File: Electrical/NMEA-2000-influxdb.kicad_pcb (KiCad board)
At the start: 4 copper layers, 9 parts, among them J1 Conn_01x02, J2 Conn_01x02, U1 LM7805_TO220, U2 SN65HVD230-Module, U3 RTC-Module, U4 ESP32-DevKitC, U5 SD-Card-Module

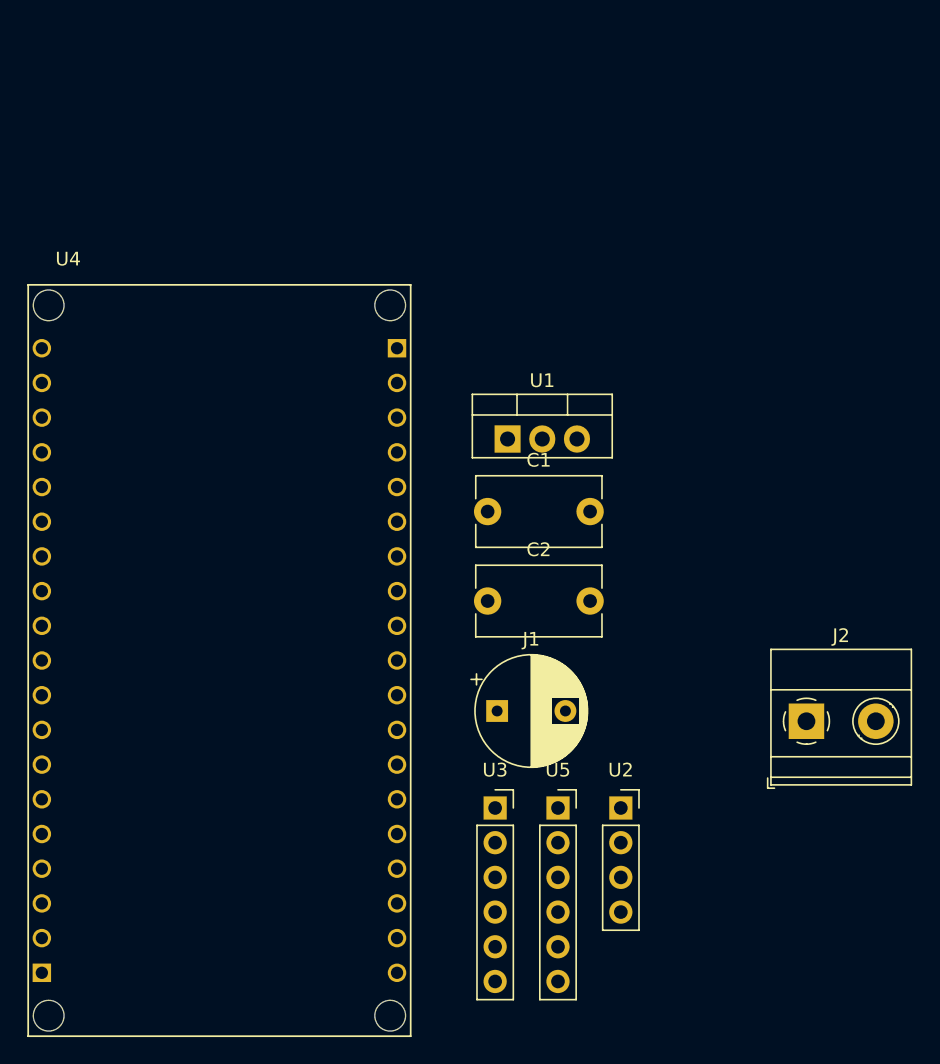
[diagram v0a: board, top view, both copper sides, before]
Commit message: Replaced SN65HVD230-Module with SN65HVD230
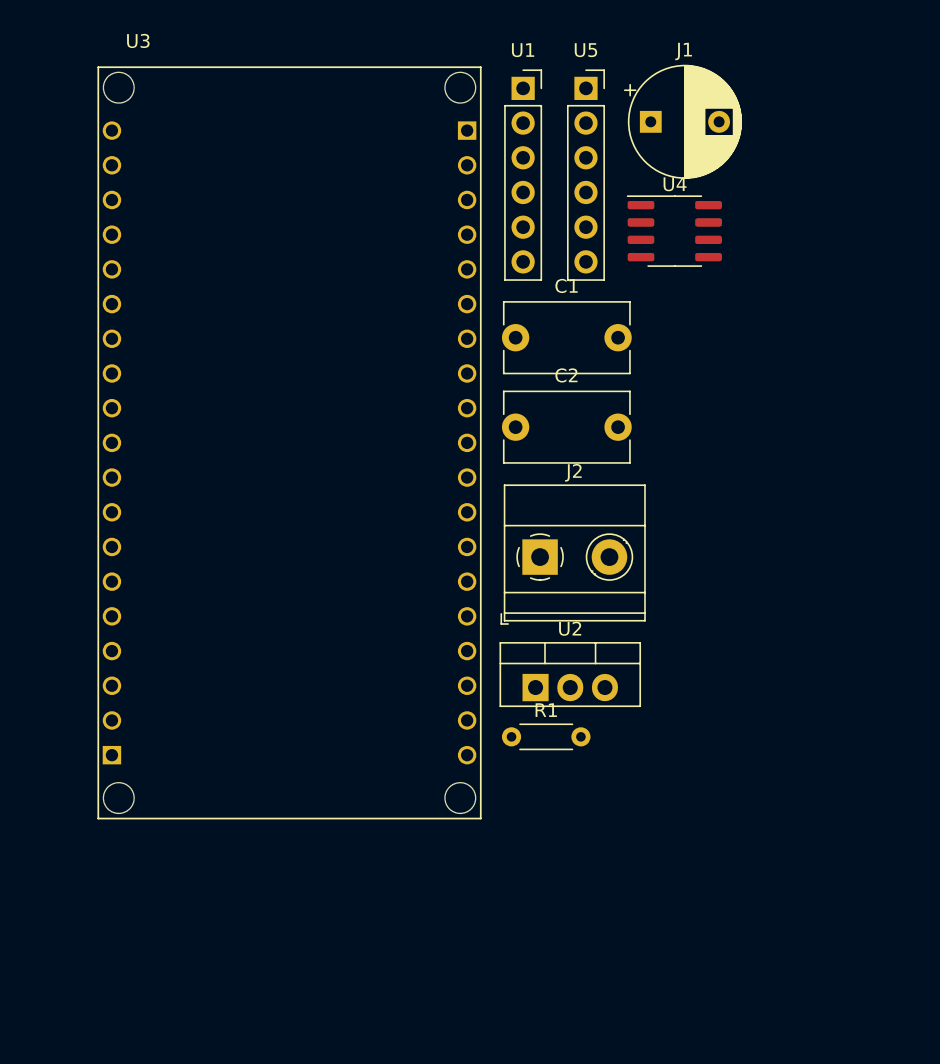
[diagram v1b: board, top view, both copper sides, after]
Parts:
- added R1: R, Resistor_THT:R_Axial_DIN0204_L3.6mm_D1.6mm_P5.08mm_Horizontal, F.Cu at (123.8, 102.9)
- U1: value LM7805_TO220 -> SD-Card-Module; footprint Package_TO_SOT_THT:TO-220-3_Vertical -> Connector_PinSocket_2.54mm:PinSocket_1x06_P2.54mm_Vertical
- U2: value SN65HVD230-Module -> LM7805_TO220; footprint Connector_PinSocket_2.54mm:PinSocket_1x04_P2.54mm_Vertical -> Package_TO_SOT_THT:TO-220-3_Vertical
- U3: value RTC-Module -> ESP32-DevKitC; footprint Connector_PinSocket_2.54mm:PinSocket_1x06_P2.54mm_Vertical -> Espressif:MODULE_ESP32_NODEMCU
- U4: value ESP32-DevKitC -> SN65HVD230; footprint Espressif:MODULE_ESP32_NODEMCU -> Package_SO:SOIC-8_3.9x4.9mm_P1.27mm
- U5: value SD-Card-Module -> RTC-Module
- moved U5 52.7 mm to (129.3, 55.4)
- moved U4 45.8 mm to (135.8, 65.8)
- moved J1 44.6 mm to (134.0, 57.9)
- moved U3 30.7 mm to (107.6, 81.3)
- moved U1 25.7 mm to (124.7, 55.4)
- moved J2 22.9 mm to (125.9, 89.7)
- moved C2 12.9 mm to (124.1, 80.2)
- moved C1 12.9 mm to (124.1, 73.7)
- moved U2 10.8 mm to (125.6, 99.3)
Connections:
- U1 pad 1: +12V -> GND
- U1 pad 2: GND -> +5V
- U1 pad 3: +5V -> /MISO
- U2 pad 1: +3V3 -> +12V
- U2 pad 3: /CAN_RX -> +5V
- U5 pad 1: GND -> +5V
- U5 pad 2: +5V -> GND
- U5 pad 3: /MISO -> (no net)
- U5 pad 4: /MOSI -> /SCL
- U5 pad 5: /SCK -> unconnected-(U5-SQW-Pad5)
- U5 pad 6: /CS -> unconnected-(U5-32K-Pad6)

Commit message: Added board
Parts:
- J1: value Conn_01x02 -> Conn_01x04; footprint Capacitor_THT:CP_Radial_D8.0mm_P5.00mm -> TerminalBlock_Phoenix:TerminalBlock_Phoenix_MKDS-1,5-4-5.08_1x04_P5.08mm_Horizontal
- J2: value Conn_01x02 -> Conn_01x04; footprint TerminalBlock_Phoenix:TerminalBlock_Phoenix_MKDS-1,5-2-5.08_1x02_P5.08mm_Horizontal -> Connector_PinSocket_2.54mm:PinSocket_1x04_P2.54mm_Horizontal
- U1, U5: footprint Connector_PinSocket_2.54mm:PinSocket_1x06_P2.54mm_Vertical -> Connector_PinSocket_2.54mm:PinSocket_1x06_P2.54mm_Horizontal
- U3: value ESP32-DevKitC -> ESP32_NODEMCU; footprint Espressif:MODULE_ESP32_NODEMCU -> esp32:esp32
- moved U2 59.6 mm to (109.2, 41.9), turned to -90 degrees
- moved U1 46.9 mm to (153.1, 92.7), turned to 180 degrees
- moved U4 45.3 mm to (100.3, 94.0)
- moved J1 39.6 mm to (97.8, 41.9), turned to -90 degrees
- moved J2 31.8 mm to (102.2, 68.5)
- moved R1 26.1 mm to (97.8, 104.1)
- moved U3 26.1 mm to (132.1, 72.4), turned to 90 degrees
- moved U5 24.8 mm to (153.1, 62.2), turned to 180 degrees
- moved C1 21.5 mm to (114.2, 54.6), turned to 180 degrees
- moved C2 19.4 mm to (114.2, 63.5), turned to 180 degrees
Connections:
- J1 pad 2: GND -> CAN_L
- J2 pad 1: Net-(J2-Pin_1) -> +5V
- J2 pad 2: Net-(J2-Pin_2) -> /RX
- U4 pad 6: Net-(J2-Pin_2) -> CAN_L
- U4 pad 7: Net-(J2-Pin_1) -> CAN_H
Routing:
- net /CAN_RX: track 0.00 -> 59.8 mm, vias 0 -> 1
- net CAN_L: track 0.00 -> 57.7 mm
- net /CAN_TX: track 0.00 -> 56.5 mm, vias 0 -> 1
- net CAN_H: track 0.00 -> 47.4 mm
- net /SCL: track 0.00 -> 46.0 mm
- net /MISO: track 0.00 -> 34.4 mm
- net /MOSI: track 0.00 -> 34.4 mm
- net /CS: track 0.00 -> 34.3 mm
- net +12V: track 0.00 -> 27.0 mm
- net /SCK: track 0.00 -> 13.6 mm
- net Net-(U4-Rs): track 0.00 -> 12.1 mm, vias 0 -> 1
- net +3.3V: track 0.00 -> 11.1 mm
- added copper zone on B.Cu, net +5V
- added copper zone on F.Cu, net GND
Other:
- board outline added: 114.3 x 71.1 mm

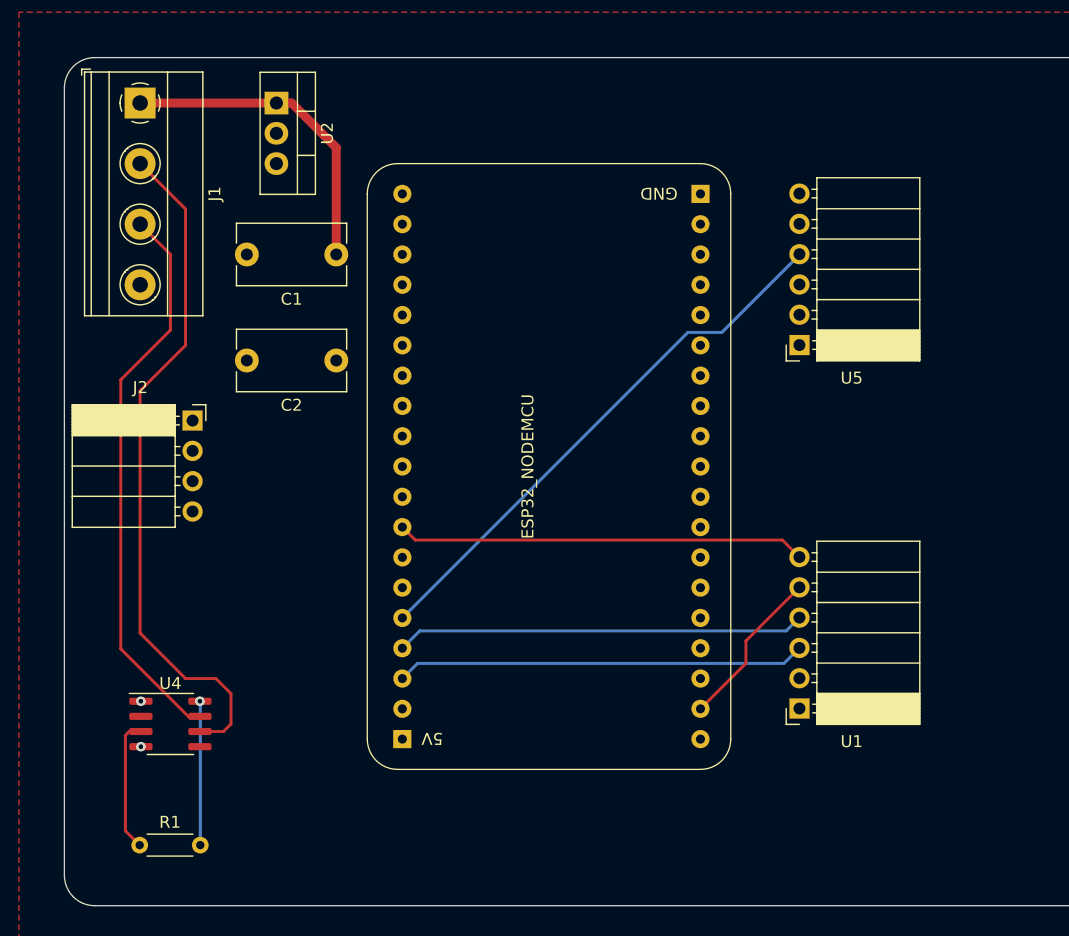
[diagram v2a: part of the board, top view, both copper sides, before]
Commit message: Updated board and added heatsink
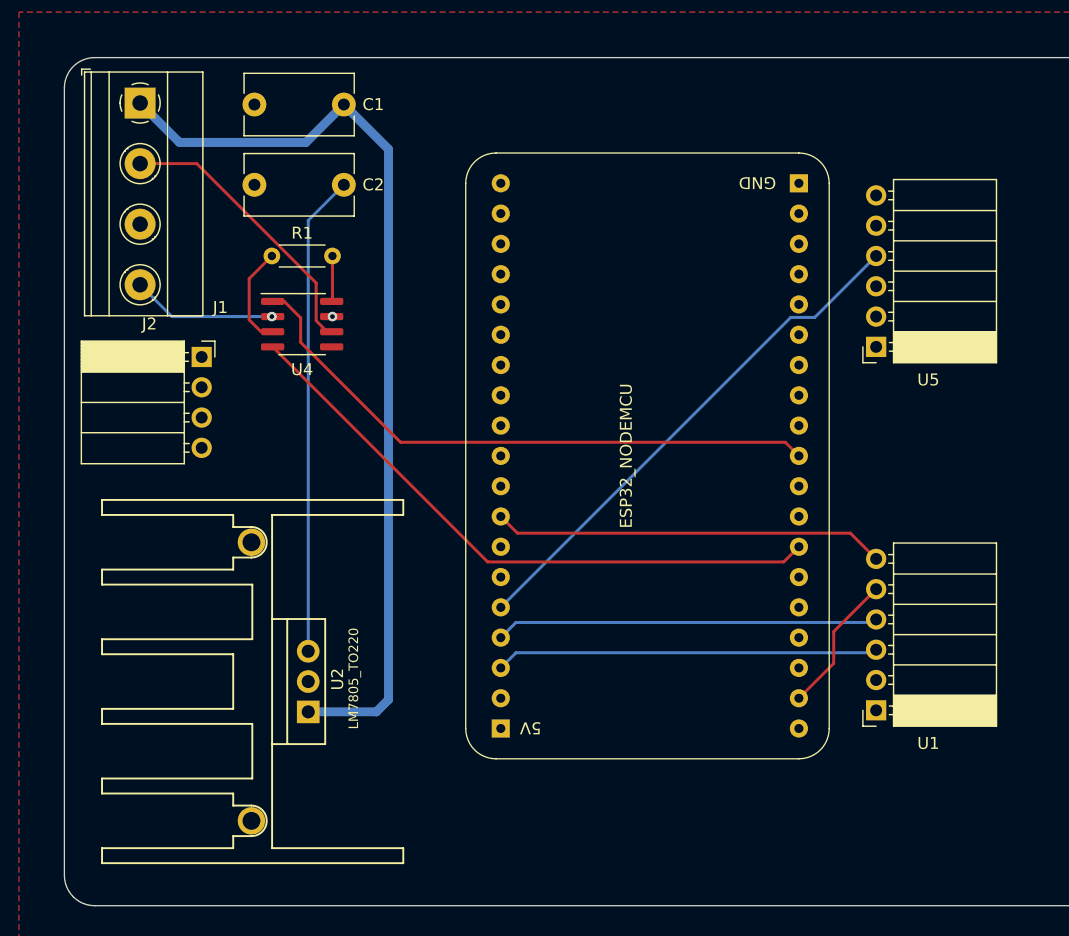
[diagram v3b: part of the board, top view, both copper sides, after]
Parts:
- U2: footprint Package_TO_SOT_THT:TO-220-3_Vertical -> Heatsinks:Heatsink_TO220-3_30x25x25mm
- moved U2 51.1 mm to (111.9, 93.0), turned to 90 degrees
- moved R1 50.6 mm to (108.8, 54.7)
- moved U4 35.3 mm to (111.4, 60.5)
- moved C2 14.7 mm to (114.9, 48.8)
- moved C1 12.6 mm to (114.9, 42.0)
- moved U3 8.30 mm to (140.3, 71.5)
- moved U1 6.43 mm to (159.5, 92.8)
- moved U5 6.43 mm to (159.5, 62.4)
- moved J2 5.39 mm to (103.0, 63.2)
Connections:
- U5 pad 3: (no net) -> /SDA
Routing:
- net /RX: track 0.00 -> 68.1 mm
- net /TX: track 0.00 -> 55.1 mm
- net +12V: track 27.0 -> 78.4 mm
- net /SDA: track 0.00 -> 40.5 mm
- net +5V: track 0.00 -> 40.4 mm
- net CAN_L: track 57.7 -> 24.6 mm
- net CAN_H: track 47.4 -> 19.4 mm, vias 0 -> 1
- net GND: track 0.00 -> 12.2 mm, vias 0 -> 1
- net /CAN_RX: track 59.8 -> 50.7 mm, vias 1 -> 0
- net Net-(U4-Rs): track 12.1 -> 3.84 mm, vias 1 -> 0
- net /CAN_TX: track 56.5 -> 52.1 mm, vias 1 -> 0
- net +3.3V: track 11.1 -> 8.53 mm
- net /SCL: track 46.0 -> 43.7 mm
- net /MISO: track 34.4 -> 32.1 mm
- net /MOSI: track 34.4 -> 32.1 mm
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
